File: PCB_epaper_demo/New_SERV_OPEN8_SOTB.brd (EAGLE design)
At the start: 126.5 x 109.5 mm, 71 parts, among them IC2 LT3082EST#PBF, IC3 RP105x, IC4 SN74AUP1G00DCKR, IC5 SN74AUP1G00DCKR, IC6 LM358AMX_NOPB, J1 TB006-508-02BE, J2 TB006-508-02BE, U1 SN74LVC1G32DBVR, U3 SN74AUP1G14DBVR, Y1 KC7050A48.0000C50D00

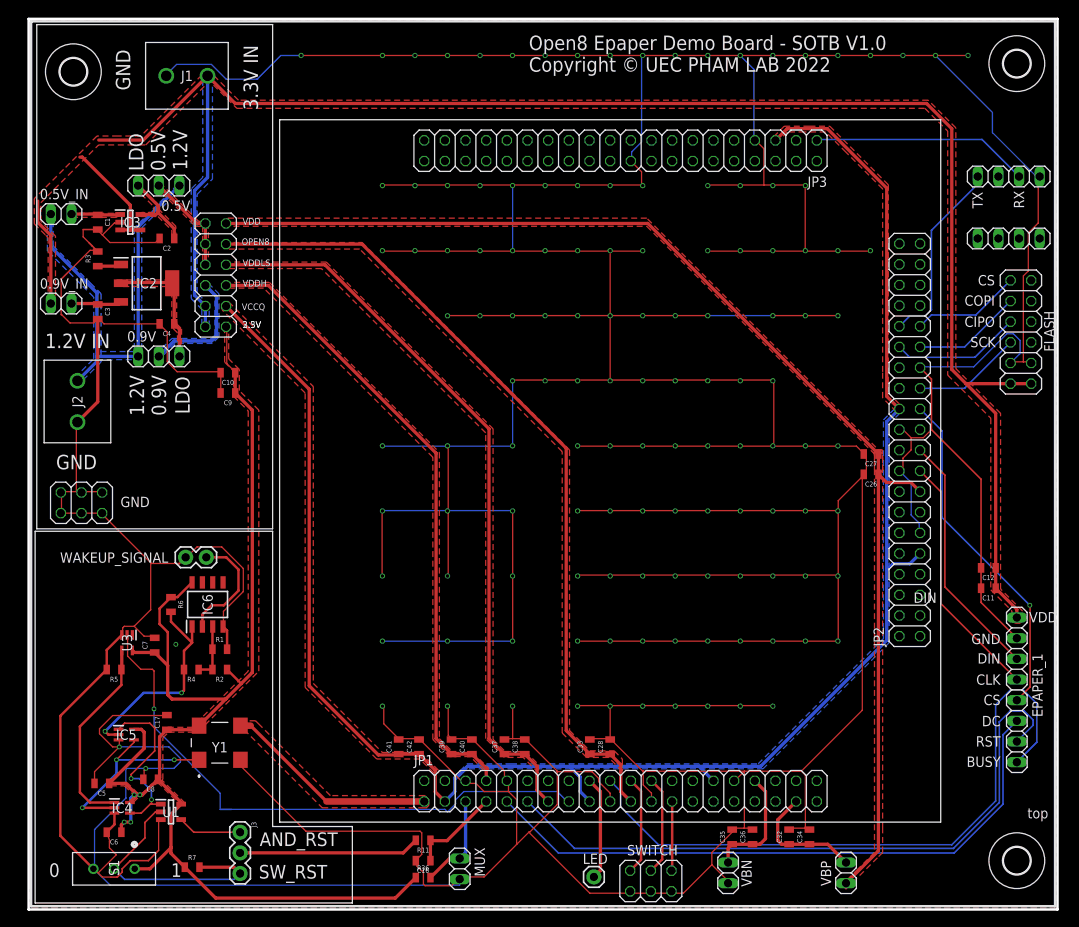
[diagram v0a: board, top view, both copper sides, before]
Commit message: add trimmer
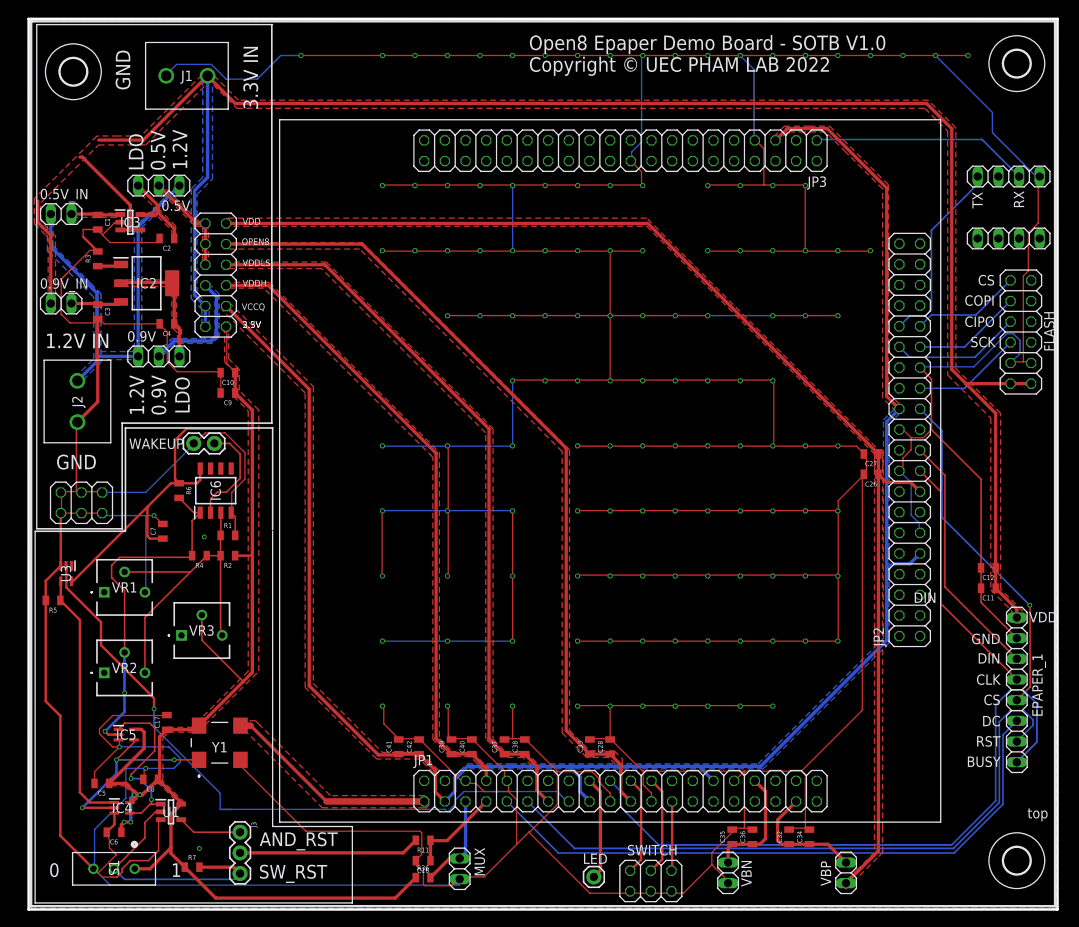
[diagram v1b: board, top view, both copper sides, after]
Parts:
- removed WAKEUP_SIGNAL: (no value), SparkFun-Connectors:1X02
- added VR1, VR2, VR3: GF063PB103K, SamacSys_Parts:GF063PB103K
- added WAKEUP: (no value), SparkFun-Connectors:1X02
- moved C7 14.0 mm to (-55.0, -12.5)
- moved IC6 14.0 mm to (-48.5, -7.50)
- moved R1 14.0 mm to (-47.0, -13.0)
- moved R2 14.0 mm to (-47.0, -15.5)
- moved R4 14.0 mm to (-50.5, -15.5)
- moved R6 14.0 mm to (-53.0, -7.50)
- moved U3 11.3 mm to (-66.9, -17.7)
- moved R5 11.3 mm to (-68.5, -21.0)
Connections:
- net GND: now also VR1.3, WAKEUP.1; no longer WAKEUP_SIGNAL.1
- net N$4: now also VR1.2, VR2.3, VR3.3
- net VDD_3.3V: now also VR3.2
- net WAKEUP_SIGNAL: now also WAKEUP.2; no longer WAKEUP_SIGNAL.2
- net WS_OPAMP: now also VR2.2
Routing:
- net N$4: track 7.00 -> 42.6 mm
- net VDD_3.3V: track 169.6 -> 194.3 mm
- net WS_OPAMP: track 26.7 -> 43.3 mm
- net GND: track 1302.5 -> 1318.5 mm, vias 130 -> 132
- net DR_ALL_LEDS[2]: track 71.8 -> 82.6 mm
- net RESET: track 24.4 -> 31.9 mm
- net WAKEUP_SIGNAL: track 14.3 -> 13.1 mm
